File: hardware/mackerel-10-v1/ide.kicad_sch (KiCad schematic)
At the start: 7 parts, among them J6 Conn_02x20_Odd_Even, U12 74HC245, U13 74HC245

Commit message: Rough layout of components on PCB
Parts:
- added J14: Screw_Terminal_01x04, TerminalBlock:TerminalBlock_bornier-4_P5.08mm, symbol Connector:Screw_Terminal_01x04
- added R17: R, Resistor_THT:R_Axial_DIN0207_L6.3mm_D2.5mm_P7.62mm_Horizontal, symbol Device:R
- D1: renamed from D5; footprint (none) -> LED_THT:LED_D5.0mm
- R14: renamed from R37; footprint (none) -> Resistor_THT:R_Axial_DIN0207_L6.3mm_D2.5mm_P7.62mm_Horizontal
- R15: renamed from R38; footprint (none) -> Resistor_THT:R_Axial_DIN0207_L6.3mm_D2.5mm_P7.62mm_Horizontal
- R16: renamed from R39; footprint (none) -> Resistor_THT:R_Axial_DIN0207_L6.3mm_D2.5mm_P7.62mm_Horizontal
- renumbered J6 to J3
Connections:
- net +5V: now also R17.1
- net /IDE_CS1: no longer J3.38 (Pin_38)
- new net: J3.38 (Pin_38), R17.2

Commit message: Settled on mini ITX form factor
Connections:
- net +5V: now also J14.4 (Pin_4)
- net GND: now also J14.2 (Pin_2), J14.3 (Pin_3)
- net +12V: now reaches J14.1 (Pin_1)
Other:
- note removed: "TODO 12v power"

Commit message: Mostly routed except expansion
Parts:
- added C43: 1000uF, Capacitor_THT:CP_Radial_D10.0mm_P5.00mm, symbol Device:C_Polarized
- added C44: 470uF, Capacitor_THT:CP_Radial_D8.0mm_P3.50mm, symbol Device:C_Polarized_US
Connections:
- net +12V: now also C43.1
- net +5V: now also C44.1
- net GND: now also C43.2, C44.2

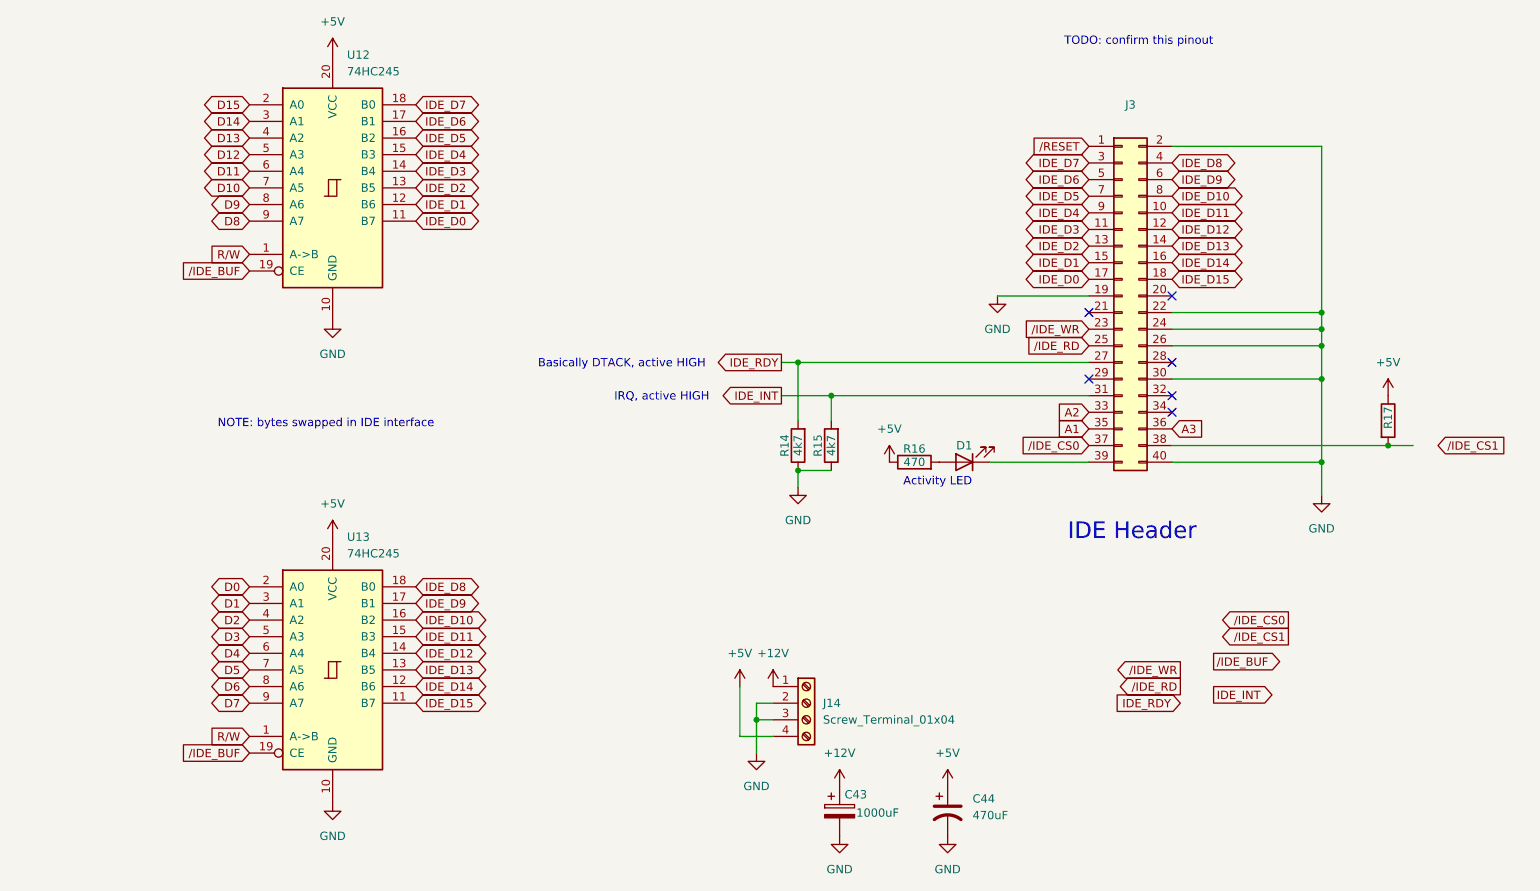
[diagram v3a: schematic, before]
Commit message: IDE interface routed
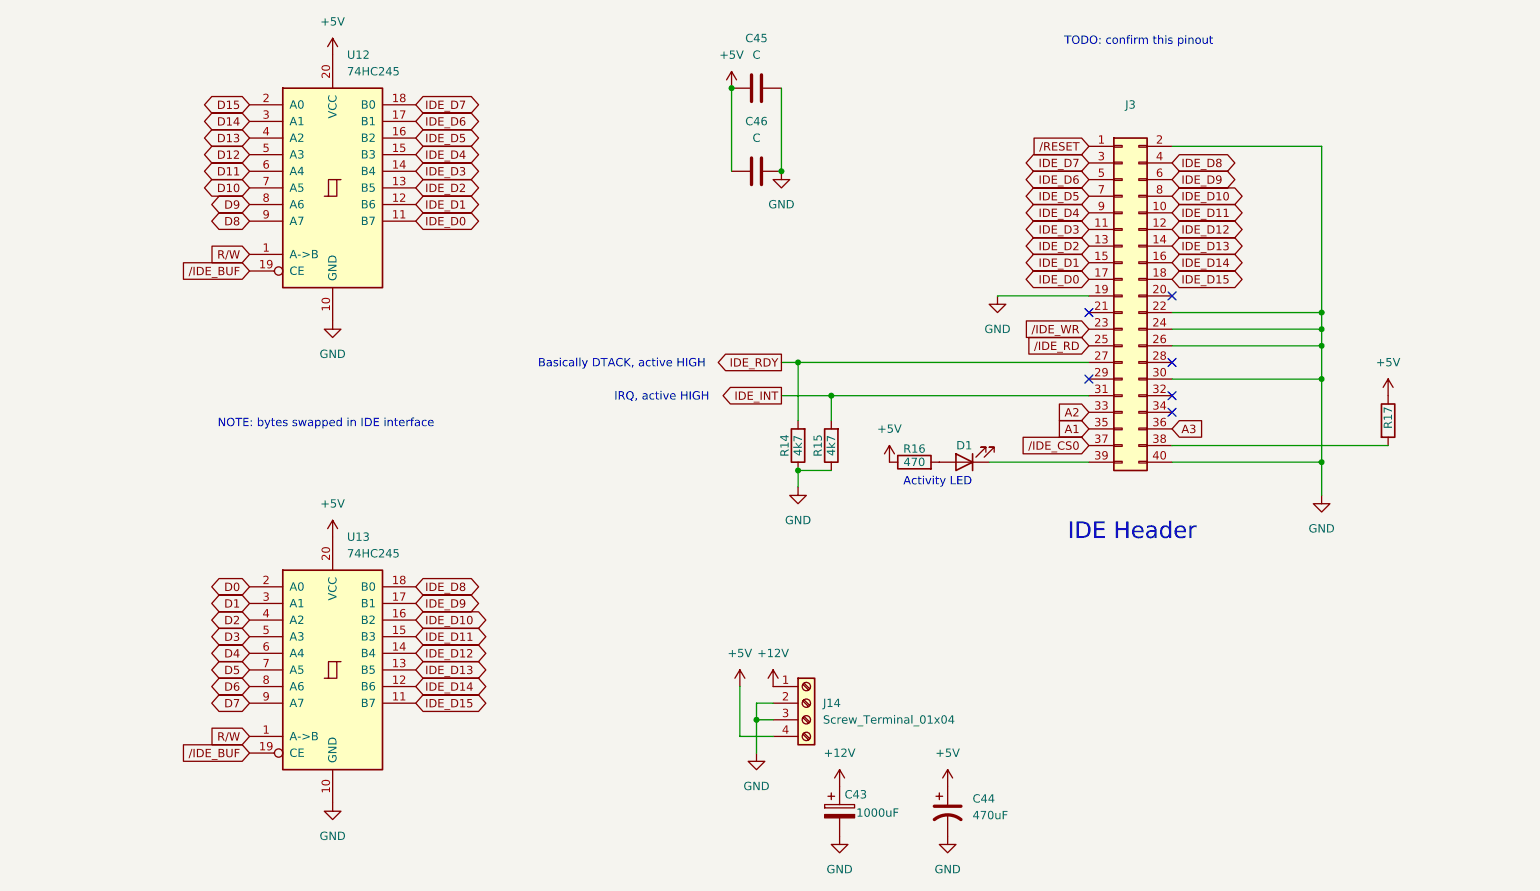
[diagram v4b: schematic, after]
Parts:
- added C45, C46: C, Capacitor_THT:C_Disc_D4.3mm_W1.9mm_P5.00mm, symbol Device:C
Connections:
- net +5V: now also C45.1, C46.1
- net GND: now also C45.2, C46.2

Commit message: Mackerel-10 v1 release
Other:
- note removed: "TODO: confirm this pinout"
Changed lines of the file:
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@@
-		)
-	)
-	(text "TODO: confirm this pinout"
-		(exclude_from_sim no)
-		(at 191.77 32.258 0)
-		(effects
-			(font
-				(size 1.27 1.27)
-			)
 		)
 	)

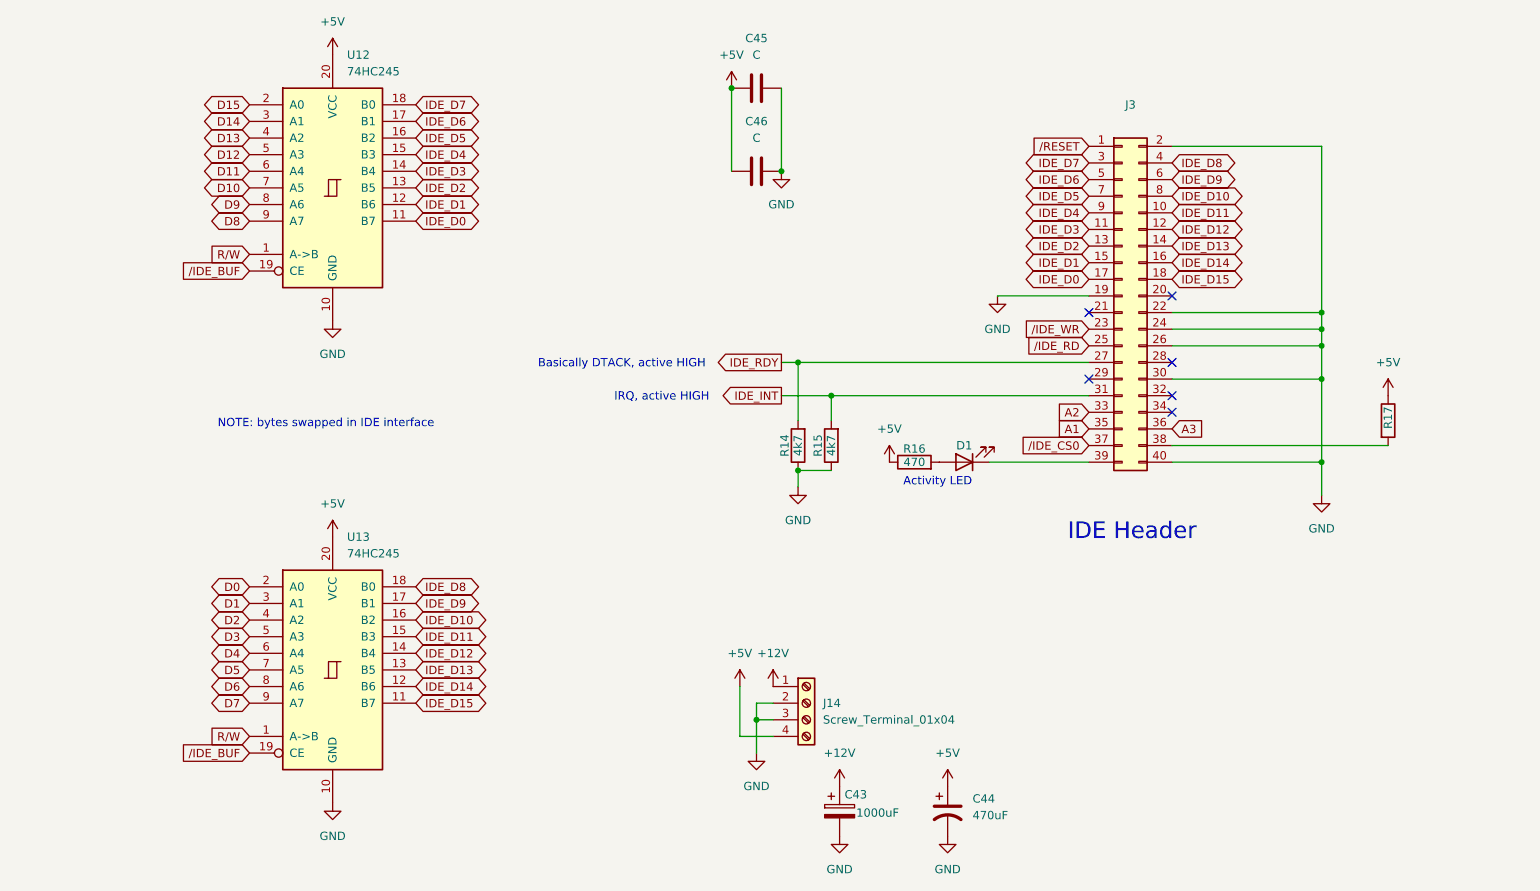
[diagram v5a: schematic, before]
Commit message: Fix IDE buffer direction and add CS1 pin
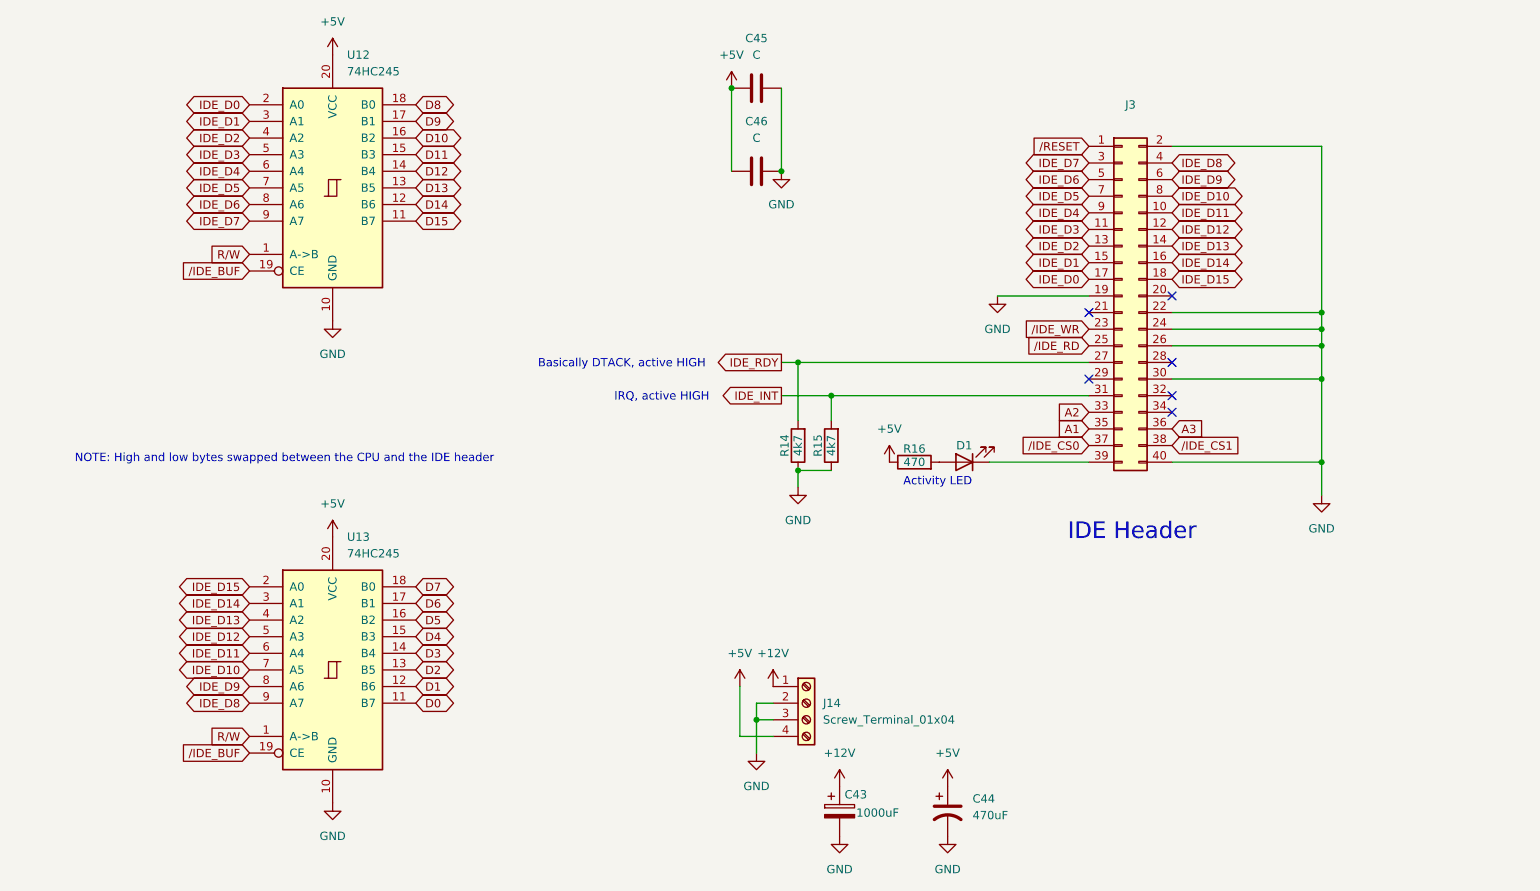
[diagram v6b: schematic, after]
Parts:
- removed R17: R, Resistor_THT:R_Axial_DIN0207_L6.3mm_D2.5mm_P7.62mm_Horizontal, symbol Device:R
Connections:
- net D0: now also U13.11 (B7); no longer U13.2 (A0)
- net D1: now also U13.12 (B6); no longer U13.3 (A1)
- net D10: now also U12.16 (B2); no longer U12.7 (A5)
- net D11: now also U12.15 (B3); no longer U12.6 (A4)
- net D12: now also U12.14 (B4); no longer U12.5 (A3)
- net D13: now also U12.13 (B5); no longer U12.4 (A2)
- net D14: now also U12.12 (B6); no longer U12.3 (A1)
- net D15: now also U12.11 (B7); no longer U12.2 (A0)
- net D2: now also U13.13 (B5); no longer U13.4 (A2)
- net D3: now also U13.14 (B4); no longer U13.5 (A3)
- net D4: now also U13.15 (B3); no longer U13.6 (A4)
- net D5: now also U13.16 (B2); no longer U13.7 (A5)
- net D6: now also U13.17 (B1); no longer U13.8 (A6)
- net D7: now also U13.18 (B0); no longer U13.9 (A7)
- net D8: now also U12.18 (B0); no longer U12.9 (A7)
- net D9: now also U12.17 (B1); no longer U12.8 (A6)
- net IDE_D0: now also U12.2 (A0); no longer U12.11 (B7)
- net IDE_D1: now also U12.3 (A1); no longer U12.12 (B6)
- net IDE_D10: now also U13.7 (A5); no longer U13.16 (B2)
- net IDE_D11: now also U13.6 (A4); no longer U13.15 (B3)
- net IDE_D12: now also U13.5 (A3); no longer U13.14 (B4)
- net IDE_D13: now also U13.4 (A2); no longer U13.13 (B5)
- net IDE_D14: now also U13.3 (A1); no longer U13.12 (B6)
- net IDE_D15: now also U13.2 (A0); no longer U13.11 (B7)
- net IDE_D2: now also U12.4 (A2); no longer U12.13 (B5)
- net IDE_D3: now also U12.5 (A3); no longer U12.14 (B4)
- net IDE_D4: now also U12.6 (A4); no longer U12.15 (B3)
- net IDE_D5: now also U12.7 (A5); no longer U12.16 (B2)
- net IDE_D6: now also U12.8 (A6); no longer U12.17 (B1)
- net IDE_D7: now also U12.9 (A7); no longer U12.18 (B0)
- net IDE_D8: now also U13.9 (A7); no longer U13.18 (B0)
- net IDE_D9: now also U13.8 (A6); no longer U13.17 (B1)
- net /IDE_CS1: now reaches J3.38 (Pin_38)
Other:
- note added: "NOTE: High and low bytes swapped between the CPU and the IDE header"
- note removed: "NOTE: bytes swapped in IDE interface"
